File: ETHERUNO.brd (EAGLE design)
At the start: 68.6 x 53.3 mm, 94 parts, among them IC1 MC33269DT-5.0, IC3 ATMEGA16U2-MU, IC4 LM358D, IC5 ATMEGA328P TQFP32, IC6 W6100-LQFP, IC7 MCP24AA025E48, J1 DC_2_1MM, J2 USB-C-16P-16P, P2 ICSP:MAIN, P3 ICSP:USB, P4 microSD, Q1 FDN340P, Q2 2N7002, U1 HY931147C-RJ45

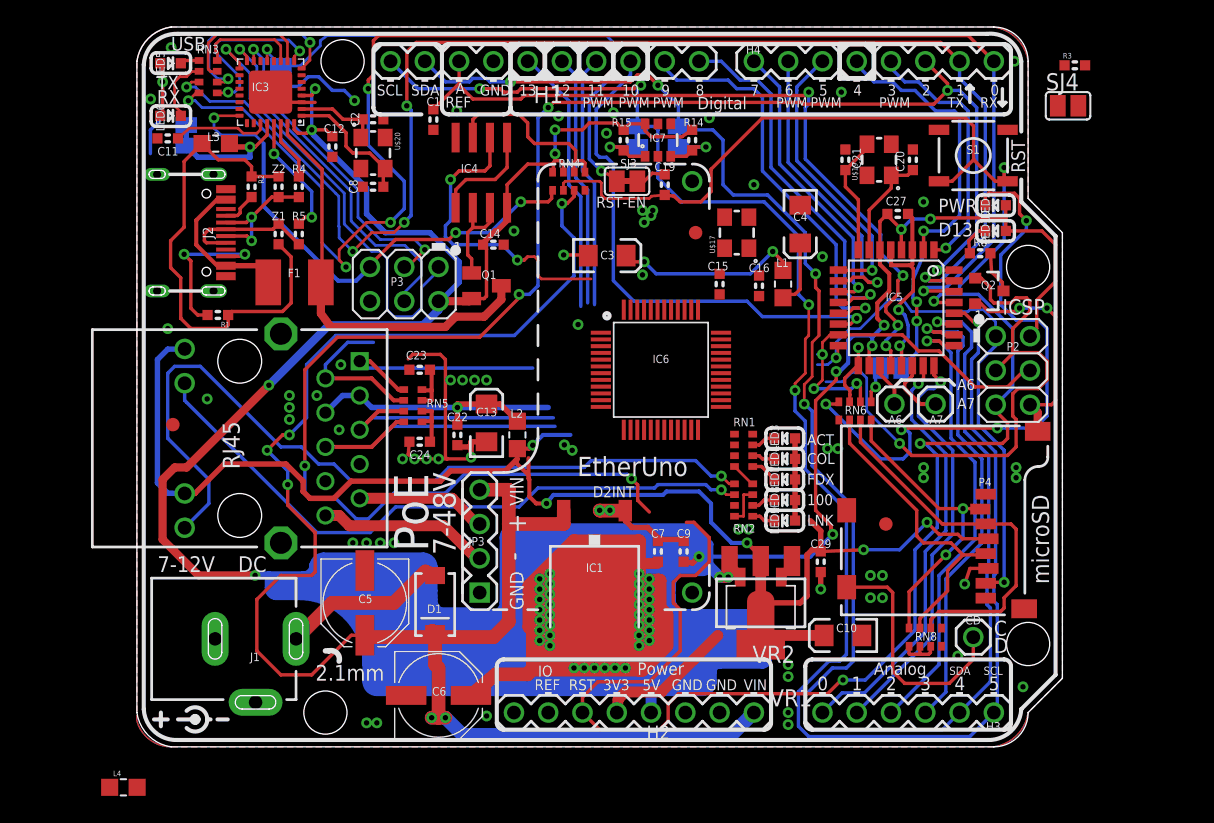
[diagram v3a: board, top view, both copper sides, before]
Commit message: Removed ATmega16U2 and added CP2102N for USB-serial conversion
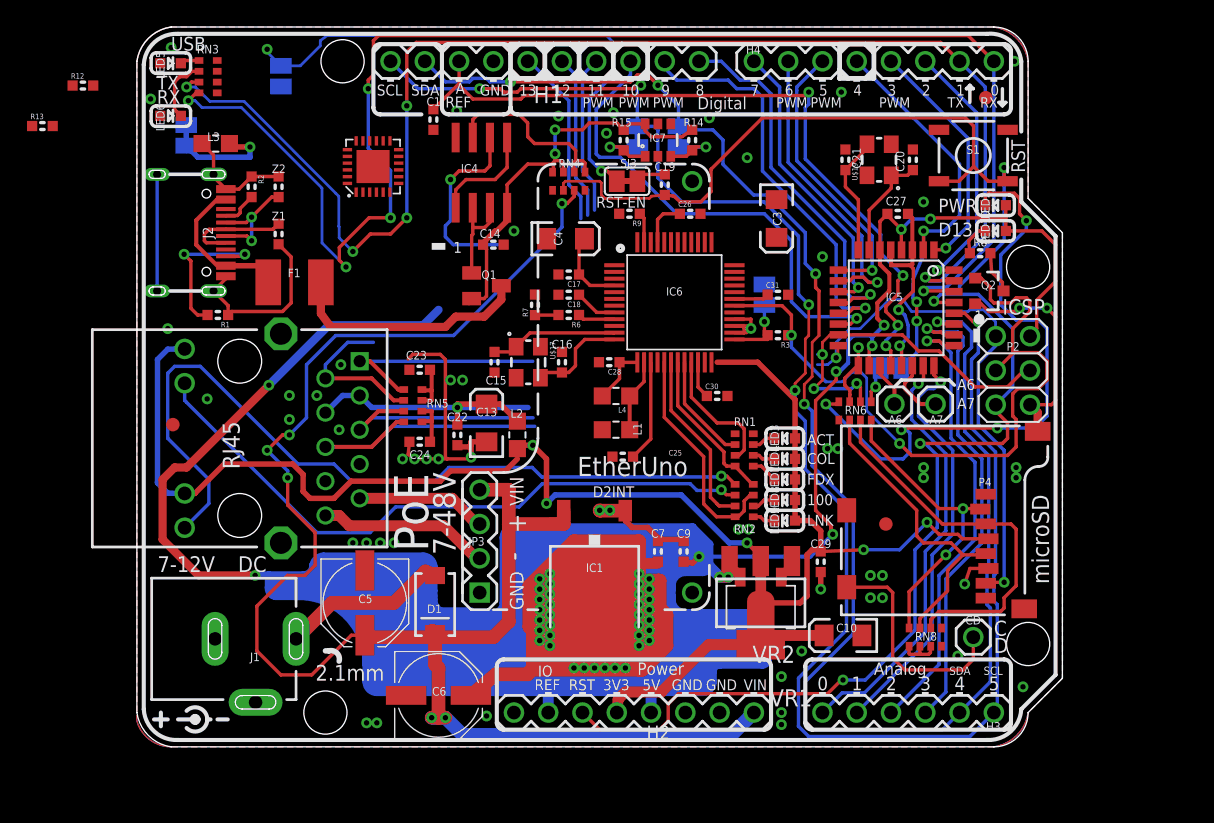
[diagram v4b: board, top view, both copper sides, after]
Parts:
- removed C11: 1uF 0603, SuperHouse-DiscreteSemi:C0603
- removed C12: 100nF 0603, SuperHouse-DiscreteSemi:C0603
- removed C2, C8: 22pF 0603, SuperHouse-DiscreteSemi:C0603
- removed IC3: ATMEGA16U2-MU, SuperHouse-MCUs:ATMEL_QFN32
- removed P3: ICSP:USB, SuperHouse-Connectors:2X03-ICSP
- removed R4, R5: 22R, SuperHouse-DiscreteSemi:R0603
- removed U$20: CRYSTAL-GND3X2, SuperHouse-Oscillators:CRYSTAL-SMD-3X2
- added C17, C18, C25, C26, C28, C30, C31: 100nF, SuperHouse-DiscreteSemi:C0603
- added IC2: CP2102N-A01-GQFN24, SuperHouse-ICs:QFN-24
- added R12: 22.1K, SuperHouse-DiscreteSemi:R0603
- added R13: 47.5K, SuperHouse-DiscreteSemi:R0603
- added R6: 12K 1%, SuperHouse-DiscreteSemi:R0603
- added R7: 300R 1%, SuperHouse-DiscreteSemi:R0603
- added R9: 10K, SuperHouse-DiscreteSemi:R0603
- R1, R2: value 4K7 -> 5K1
- R3: value (none) -> 10K
- moved L4 46.6 mm to (35.5, 26.0), turned to 180 degrees
- moved R3 29.7 mm to (47.5, 30.5), turned to 180 degrees
- moved SJ4 26.5 mm to (46.5, 33.5), flipped to the bottom, turned to 90 degrees
- moved FID1 23.7 mm to (62.9, 48.1)
- moved U$17 18.2 mm to (29.0, 28.5), turned to 270 degrees
- moved C15 17.7 mm to (26.5, 28.5), turned to 270 degrees
- moved C4 17.4 mm to (31.8, 37.6), turned to 0 degrees
- moved L1 16.4 mm to (35.5, 23.5), turned to 180 degrees
- moved C16 15.7 mm to (31.5, 28.5)
- moved C3 12.8 mm to (47.4, 39.2), turned to 270 degrees
- moved IC6 5.10 mm to (39.8, 32.9)
- moved RN2 0.06 mm to (45.0, 18.2)
- moved RN1 0.05 mm to (45.0, 22.0)
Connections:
- removed net 3V3D: C29.1, H2.4, P4.4, SJ4.2
- removed net D10_SS: H1.3, IC5.14
- removed net MISO2: IC3.17, P3.1
- removed net MOSI2: IC3.16, P3.4
- removed net N$117: C11.1, IC3.27
- removed net N$16: J2.A6, J2.B6, R5.2, Z1.1
- removed net N$17: J2.A7, J2.B7, R4.2, Z2.1
- removed net N$31: C2.2, IC3.2, U$20.1
- removed net N$33: IC6.29
- removed net N$8: C8.2, IC3.1, U$20.3
- removed net RD+: IC3.29, R5.1
- removed net RD-: IC3.30, R4.1
- removed net RESET2: IC3.24, P3.5, RN4.1
- removed net RXLED: IC3.10, RN3.7
- removed net SCK2: IC3.15, P3.3
- removed net TXLED: IC3.11, RN3.8
- new net D+: IC2.3, J2.A6, J2.B6, Z1.1
- new net D-: IC2.4, J2.A7, J2.B7, Z2.1
- new net D10_CS: H1.3, IC5.14, IC6.29
- new net N$35: R6.2, R7.1
- new net N$36: IC6.9, R6.1
- new net N$37: IC6.47, R9.1
- new net N$39: IC2.8, R12.1, R13.2
- new net RX_LED: IC2.13, RN3.7
- new net TX_LED: IC2.14, RN3.8
- net 1V2A: now also C17.1
- net 1V2D: now also C26.1, C28.1, C30.1, C31.1
- net 3.3V: now also C29.1, H2.4, IC2.5, IC2.6, IC2.7, LED5.A, LED6.A, P4.4, R9.2, SJ4.2
- net 3V3A: now also C18.1, C25.1
- net 5V: now also H2.2, R12.2; no longer C12.1, IC3.32, IC3.4, LED5.A, LED6.A, P3.2, RN4.8
- net DTR: now also IC2.23; no longer IC3.13
- net GND: now also C17.2, C18.2, C25.2, C26.2, C28.2, C30.2, C31.2, IC2.2, IC2.TGND, R13.1, R7.2; no longer C11.2, C12.2, C2.1, C8.1, IC3.3, IC3.EXP, P3.6, U$20.2, U$20.4
- net USBGND: no longer IC3.28
- net USBRXD: now also IC2.21; no longer IC3.9
- net USBTXD: now also IC2.20; no longer IC3.8
- net USBVCC: no longer IC3.31
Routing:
- net D2: track 122.9 -> 19.6 mm, vias 6 -> 1
- net D10_SS: track 38.9 -> 0.00 mm, vias 1 -> 0
- net RESET2: track 38.4 -> 0.00 mm, vias 3 -> 0
- net D10_CS: track 0.00 -> 36.4 mm, vias 0 -> 1
- net 5V: track 1210.8 -> 1175.3 mm, vias 52 -> 49
- net 3.3V: track 108.7 -> 143.7 mm, vias 5 -> 6
- net 3V3D: track 34.7 -> 0.00 mm, vias 2 -> 0
- net MISO2: track 33.0 -> 0.00 mm, vias 1 -> 0
- net MOSI2: track 27.1 -> 0.00 mm, vias 1 -> 0
- net SCK2: track 24.5 -> 0.00 mm, vias 2 -> 0
- net RESET: track 147.7 -> 125.5 mm
- net USBTXD: track 14.9 -> 0.00 mm, vias 2 -> 0
- net LINKLED: track 3.06 -> 16.9 mm
- net USBRXD: track 13.4 -> 0.08 mm, vias 2 -> 0
- net 1V2D: track 0.00 -> 13.2 mm
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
